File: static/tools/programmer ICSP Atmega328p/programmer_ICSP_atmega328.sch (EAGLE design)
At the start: 5 parts, among them IC1 MEGA8-P

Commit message: [Programmer ICSP Atmega328p] optimise routing
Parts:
- added LED1: (no value), led:LED3MM
- added R1, R2: (no value), rcl:R-EU_0207/7
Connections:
- new net JUJU: LED1.A, R2.2
- net GND: now also LED1.C
- net N$2: now also R1.1
- net N$3: now also R2.1
- net VCC: now also R1.2
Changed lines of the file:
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@@
 <part name="C1" library="capacitor-wima" deviceset="C" device="5/5"/>
 <part name="C2" library="capacitor-wima" deviceset="C" device="5/5"/>
+<part name="R1" library="rcl" deviceset="R-EU_" device="0207/7"/>
+<part name="R2" library="rcl" deviceset="R-EU_" device="0207/7"/>
+<part name="LED1" library="led" deviceset="LED" device="3MM"/>
 </parts>
 <sheets>
@@
 <instance part="C1" gate="G$1" x="-22.86" y="86.36" rot="R90"/>
 <instance part="C2" gate="G$1" x="-22.86" y="96.52" rot="R90"/>
+<instance part="R1" gate="G$1" x="-12.7" y="127" rot="R90"/>
+<instance part="R2" gate="G$1" x="63.5" y="53.34"/>
+<instance part="LED1" gate="G$1" x="71.12" y="53.34" rot="R90"/>
 </instances>
 <busses>
@@
 <junction x="-25.4" y="91.44"/>
 </segment>
+<segment>
+<pinref part="LED1" gate="G$1" pin="C"/>
+<wire x1="76.2" y1="53.34" x2="78.74" y2="53.34" width="0.1524" layer="91"/>
+<label x="78.74" y="53.34" size="1.778" layer="95"/>
+</segment>
 </net>
 <net name="VCC" class="0">
@@
 <label x="-12.7" y="76.2" size="1.778" layer="95"/>
 </segment>
+<segment>
+<pinref part="R1" gate="G$1" pin="2"/>
+<wire x1="-12.7" y1="132.08" x2="-12.7" y2="134.62" width="0.1524" layer="91"/>
+<label x="-12.7" y="137.16" size="1.778" layer="95"/>
+</segment>
 </net>
 <net name="N$1" class="0">
@@
 <segment>
 <wire x1="86.36" y1="83.82" x2="48.26" y2="121.92" width="0.1524" layer="91"/>
-<wire x1="48.26" y1="121.92" x2="-10.16" y2="121.92" width="0.1524" layer="91"/>
-<wire x1="-10.16" y1="121.92" x2="-12.7" y2="119.38" width="0.1524" layer="91"/>
-<wire x1="-12.7" y1="119.38" x2="-12.7" y2="114.3" width="0.1524" layer="91"/>
+<wire x1="48.26" y1="121.92" x2="-12.7" y2="121.92" width="0.1524" layer="91"/>
+<wire x1="-12.7" y1="121.92" x2="-12.7" y2="114.3" width="0.1524" layer="91"/>
 <wire x1="-12.7" y1="114.3" x2="-10.16" y2="111.76" width="0.1524" layer="91"/>
 <pinref part="IC1" gate="G$1" pin="PC6(/RESET)"/>
@@
 <pinref part="JP1" gate="A" pin="5"/>
 <wire x1="86.36" y1="83.82" x2="99.06" y2="83.82" width="0.1524" layer="91"/>
+<pinref part="R1" gate="G$1" pin="1"/>
+<junction x="-12.7" y="121.92"/>
 </segment>
 </net>
@@
 <pinref part="JP1" gate="A" pin="7"/>
 <wire x1="99.06" y1="81.28" x2="86.36" y2="81.28" width="0.1524" layer="91"/>
+<pinref part="R2" gate="G$1" pin="1"/>
+<junction x="58.42" y="53.34"/>
 </segment>
 </net>
@@
 </segment>
 </net>
+<net name="JUJU" class="0">
+<segment>
+<pinref part="R2" gate="G$1" pin="2"/>
+<pinref part="LED1" gate="G$1" pin="A"/>
+</segment>
+</net>

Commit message: [Programmer ICSP Atmega328p] add capa values.
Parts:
- C1, C2: value (none) -> 20pF
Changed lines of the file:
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@@
 <part name="IC1" library="atmel" deviceset="MEGA8-P" device=""/>
 <part name="Q1" library="special" deviceset="XTAL/S" device=""/>
-<part name="C1" library="capacitor-wima" deviceset="C" device="5/5"/>
-<part name="C2" library="capacitor-wima" deviceset="C" device="5/5"/>
+<part name="C1" library="capacitor-wima" deviceset="C" device="5/5" value="20pF"/>
+<part name="C2" library="capacitor-wima" deviceset="C" device="5/5" value="20pF"/>
 <part name="R1" library="rcl" deviceset="R-EU_" device="0207/7"/>
 <part name="R2" library="rcl" deviceset="R-EU_" device="0207/7"/>

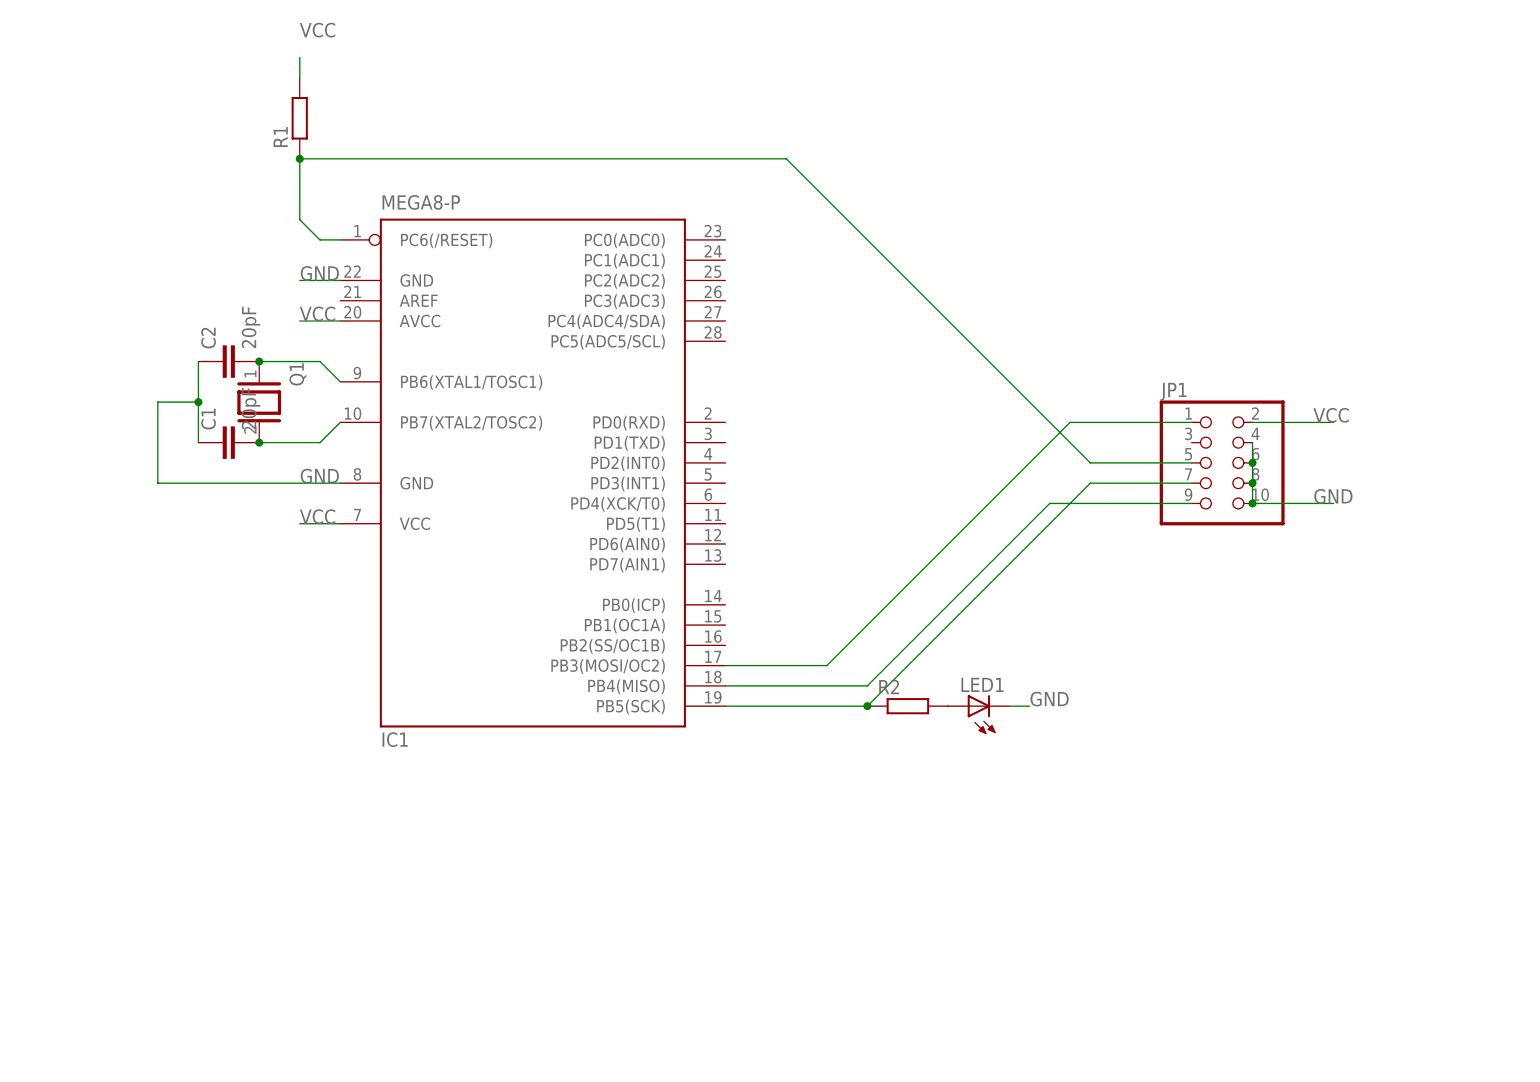
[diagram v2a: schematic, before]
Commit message: [Porgrammer ICSP] Make another design for handle Attiny85
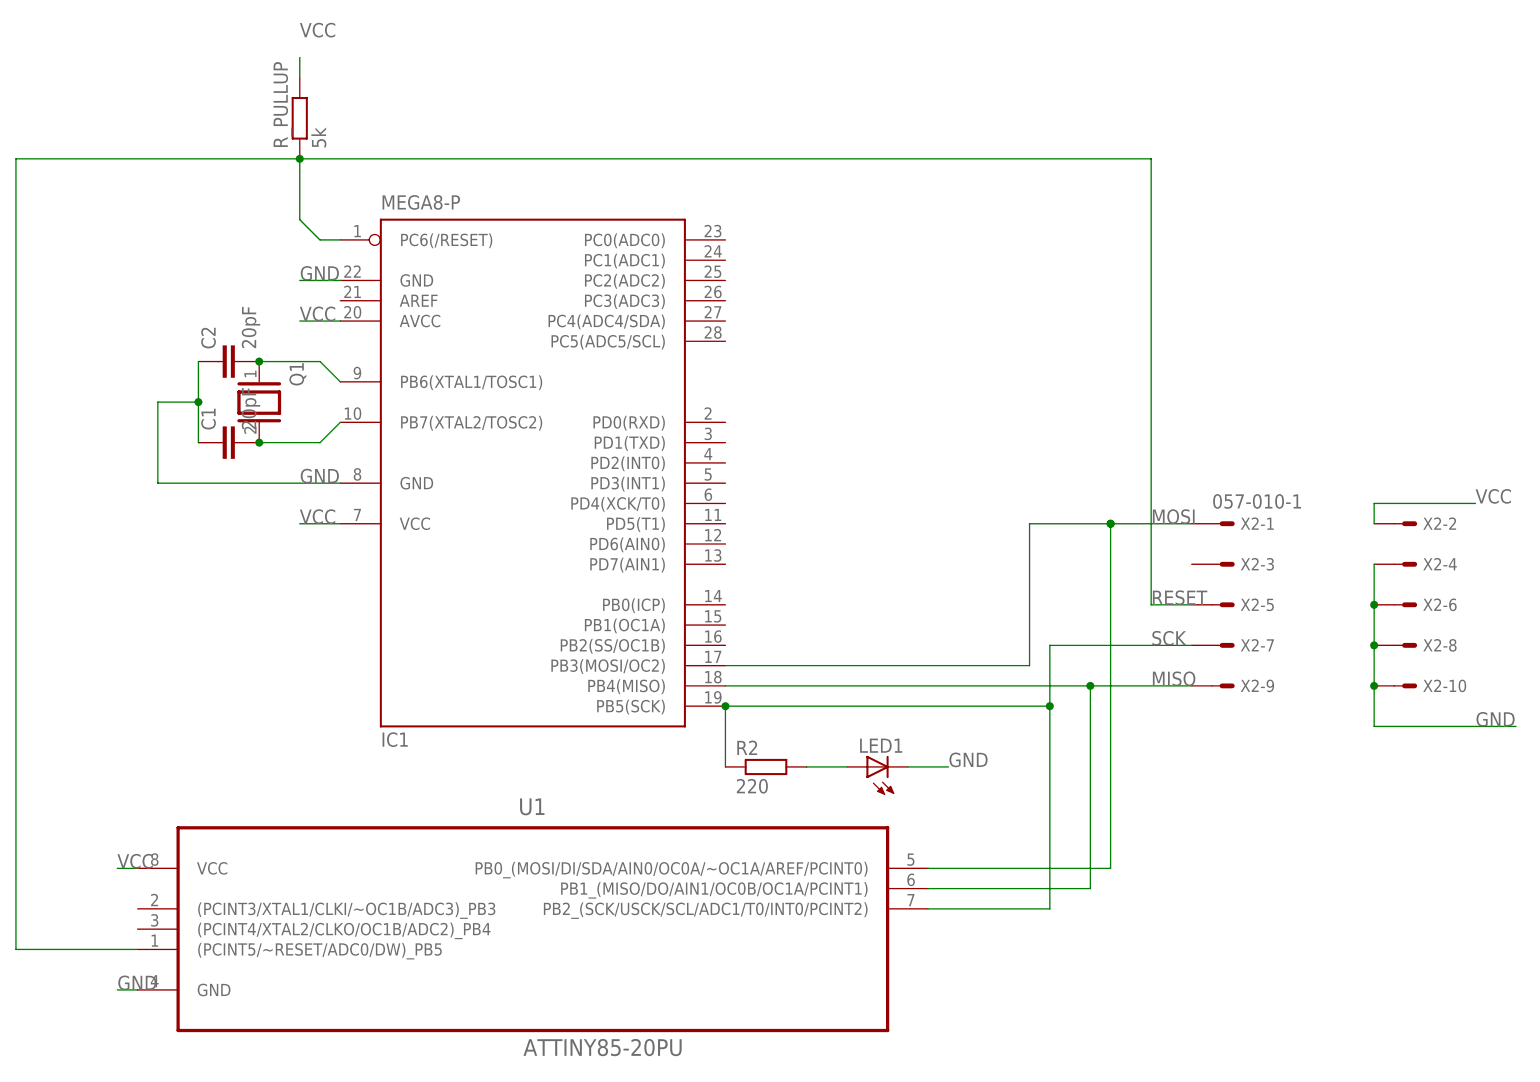
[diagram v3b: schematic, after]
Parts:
- removed JP1: (no value), pinhead:PINHD-2X5
- added U1: ATTINY85-20PU, Atmel_By_element14_Batch_1-00:ATTINY85-20PU
- added X2: 057-010-1, con-panduit:057-010-1
- R2: value (none) -> 220
- R_PULLUP: value (none) -> 5k
- renumbered R1 to R_PULLUP
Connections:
- removed net N$1: IC1.PB3(MOSI/OC2), JP1.1
- removed net N$2: IC1.PC6(/RESET), JP1.5, R_PULLUP.1
- removed net N$3: IC1.PB5(SCK), JP1.7, R2.1
- removed net N$4: IC1.PB4(MISO), JP1.9
- new net MISO: IC1.PB4(MISO), U1.PB1_(MISO/DO/AIN1/OC0B/OC1A/PCINT1), X2-9.S
- new net MOSI: IC1.PB3(MOSI/OC2), U1.PB0_(MOSI/DI/SDA/AIN0/OC0A/~OC1A/AREF/PCINT0), X2-1.S
- new net RESET: IC1.PC6(/RESET), R_PULLUP.1, U1.(PCINT5/~RESET/ADC0/DW)_PB5, X2-5.S
- new net SCK: IC1.PB5(SCK), R2.1, U1.PB2_(SCK/USCK/SCL/ADC1/T0/INT0/PCINT2), X2-7.S
- net GND: now also U1.GND, X2-10.S, X2-4.S, X2-6.S, X2-8.S; no longer JP1.10, JP1.4, JP1.6, JP1.8
- net VCC: now also U1.VCC, X2-2.S; no longer JP1.2
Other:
- moved on the sheet: LED1, R2
